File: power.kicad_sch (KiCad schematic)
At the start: 12 parts, among them Q1 Si2312BDS, U1 TLE2426xP, U2 TPS7250

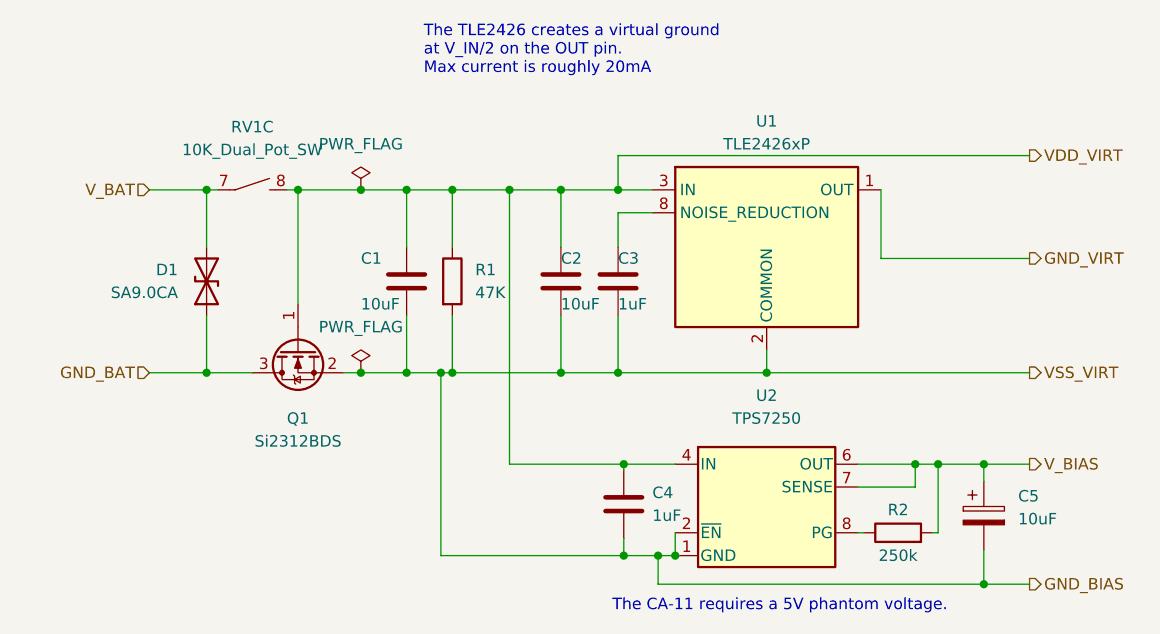
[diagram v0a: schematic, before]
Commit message: Almost finished 2-layer routing, not sure about power/ground layers though
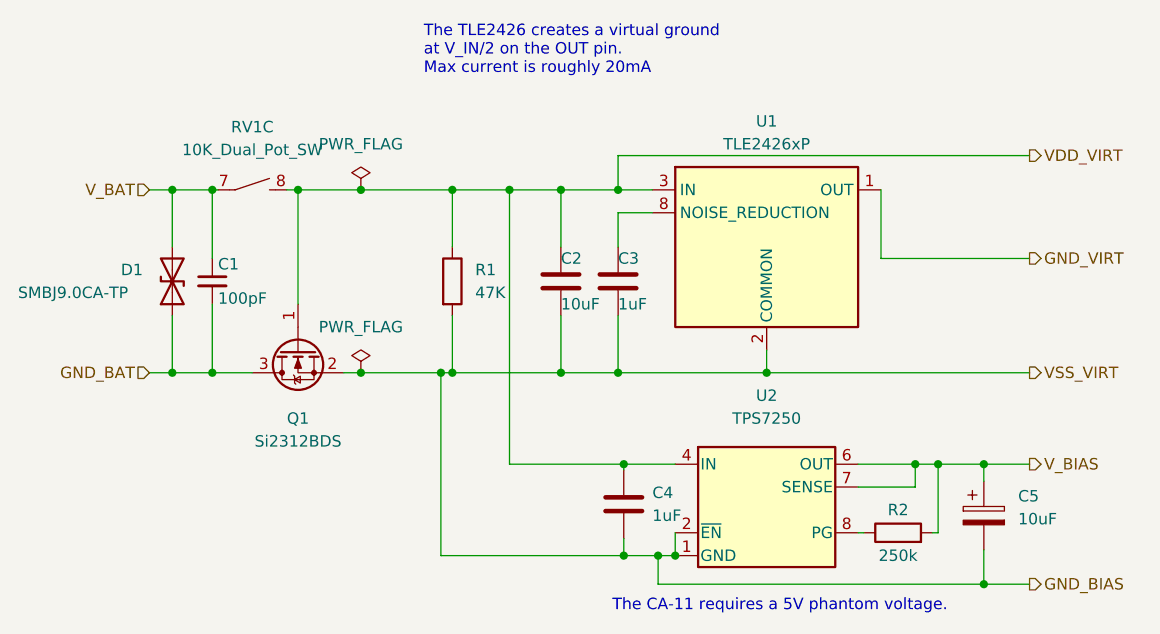
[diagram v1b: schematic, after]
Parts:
- removed C1: 10uF, Capacitor_SMD:C_1206_3216Metric, symbol Device:C
- added C1: 100pF, Capacitor_SMD:C_0603_1608Metric, symbol Device:C_Small
- D1: value SA9.0CA -> SMBJ9.0CA-TP; footprint Diode_THT:D_5KP_P7.62mm_Vertical_KathodeUp -> Diode_SMD:D_SMB_Handsoldering
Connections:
- net GND_BAT: now also C1.2
- net V_BAT: now also C1.1
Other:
- moved on the sheet: D1
